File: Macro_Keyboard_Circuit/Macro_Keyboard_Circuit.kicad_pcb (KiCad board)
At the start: 2 copper layers, 115.2 x 117.1 mm, 49 parts, among them J1 OSTTC082162, J2 PRT-16766, SW1 SW_Push, SW10 SW_Push, SW11 SW_Push, SW12 SW_Push, SW2 SW_Push, SW3 SW_Push, SW4 SW_Push, SW5 SW_Push, SW6 SW_Push, SW7 SW_Push, SW8 SW_Push, SW9 SW_Push, U1 KY-040, U2 Adafruit KB2040, U3 KY-040, U4 KY-040

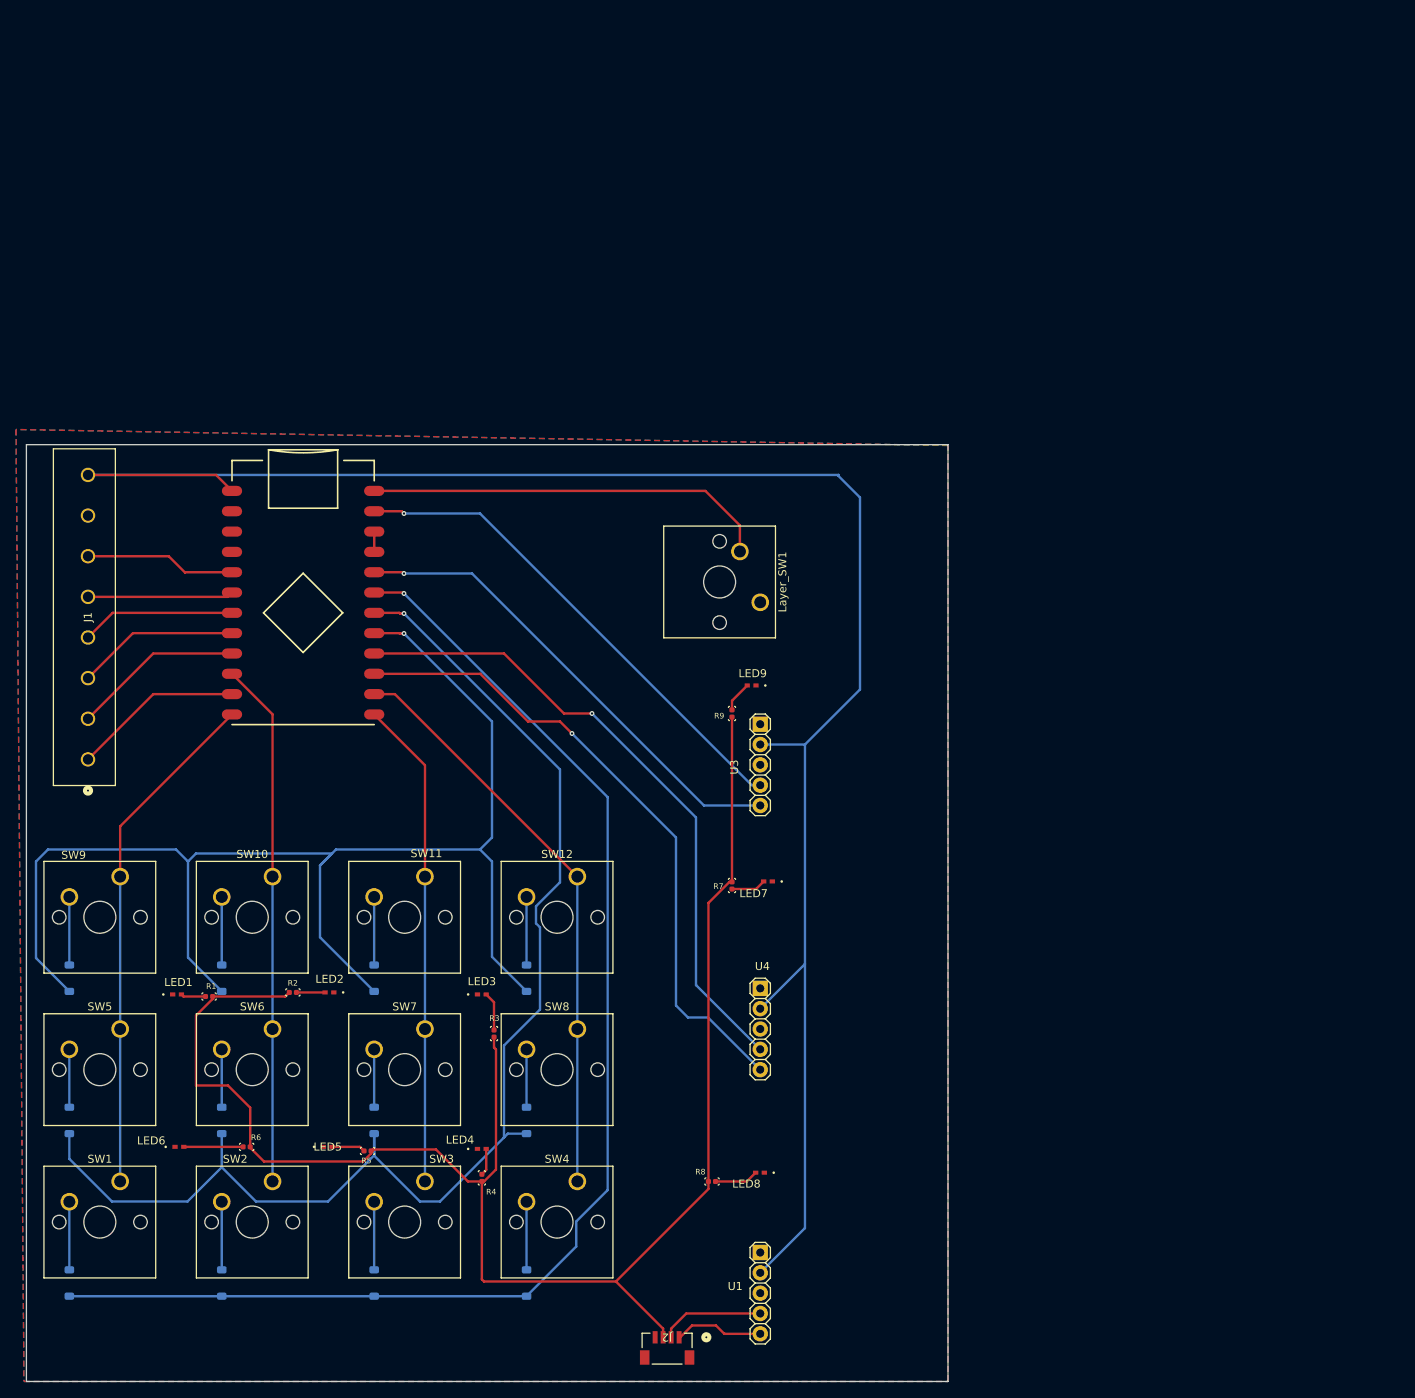
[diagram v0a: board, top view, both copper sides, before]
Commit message: Major revision to circuit due to change in acess to assembly tools. Finalized verson of PCB. Still need to update board codebase to reflect the new board configurations.
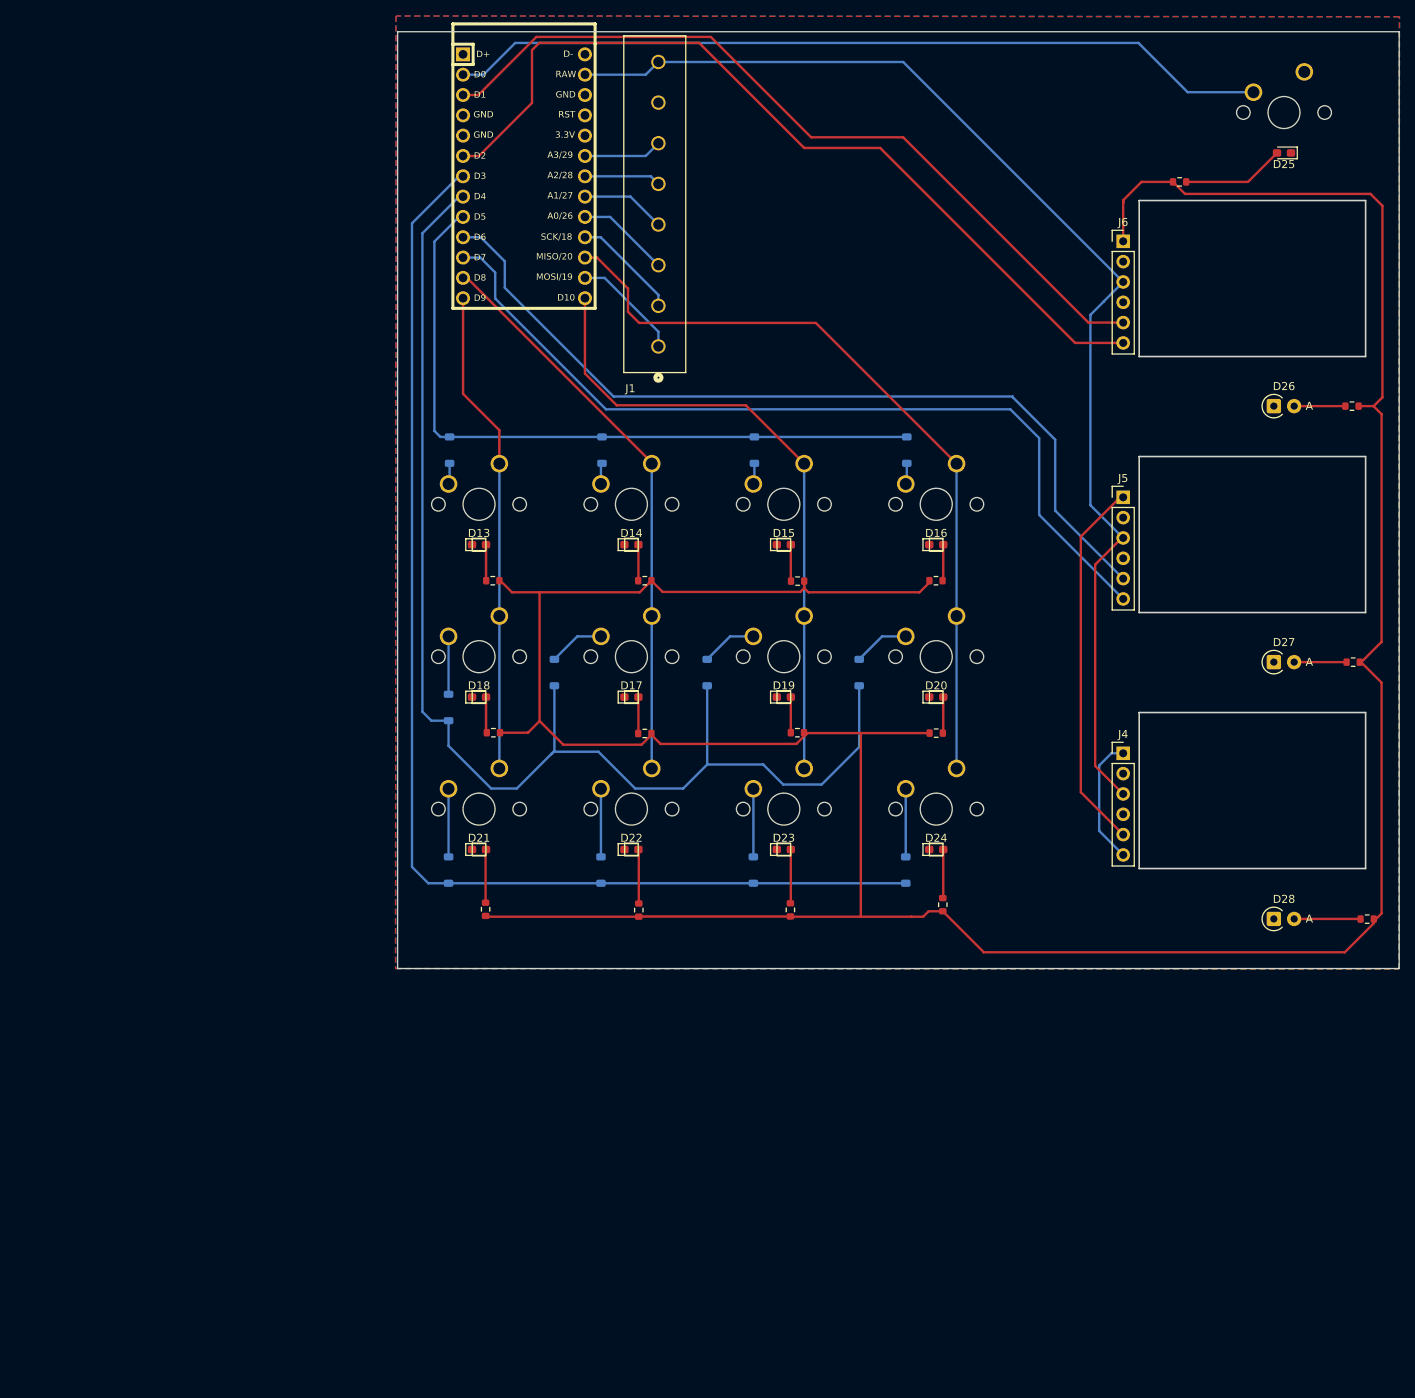
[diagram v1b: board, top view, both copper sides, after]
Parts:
- removed J2: PRT-16766, PRT_16766:CONN_BM04B-SRSS-TB_SPK
- removed LED1, LED2, LED3, LED4, LED5, LED6, LED7, LED8, LED9: HSMW-C280, HSMW_C280:LED_HSMW-C280_BRA
- removed U2: Adafruit KB2040, SparkFun-Board:ProMicroC
- removed U3, U4: KY-040, KY_040:KY_040_PORT
- added D13: LED, SW_Cherry_MX:D_0603_1608Metric_Pad1.05x0.95mm_HandSolder_cherrymx_silk, F.Cu at (77.9, 94.4)
- added D14: LED, SW_Cherry_MX:D_0603_1608Metric_Pad1.05x0.95mm_HandSolder_cherrymx_silk, F.Cu at (96.9, 94.4)
- added D15: LED, SW_Cherry_MX:D_0603_1608Metric_Pad1.05x0.95mm_HandSolder_cherrymx_silk, F.Cu at (116.0, 94.4)
- added D16: LED, SW_Cherry_MX:D_0603_1608Metric_Pad1.05x0.95mm_HandSolder_cherrymx_silk, F.Cu at (135.0, 94.4)
- added D17: LED, SW_Cherry_MX:D_0603_1608Metric_Pad1.05x0.95mm_HandSolder_cherrymx_silk, F.Cu at (96.9, 113.5)
- added D18: LED, SW_Cherry_MX:D_0603_1608Metric_Pad1.05x0.95mm_HandSolder_cherrymx_silk, F.Cu at (77.9, 113.5)
- added D19: LED, SW_Cherry_MX:D_0603_1608Metric_Pad1.05x0.95mm_HandSolder_cherrymx_silk, F.Cu at (116.0, 113.5)
- added D20: LED, SW_Cherry_MX:D_0603_1608Metric_Pad1.05x0.95mm_HandSolder_cherrymx_silk, F.Cu at (135.0, 113.5)
- added D21: LED, SW_Cherry_MX:D_0603_1608Metric_Pad1.05x0.95mm_HandSolder_cherrymx_silk, F.Cu at (77.9, 132.5)
- added D22: LED, SW_Cherry_MX:D_0603_1608Metric_Pad1.05x0.95mm_HandSolder_cherrymx_silk, F.Cu at (96.9, 132.5)
- added D23: LED, SW_Cherry_MX:D_0603_1608Metric_Pad1.05x0.95mm_HandSolder_cherrymx_silk, F.Cu at (116.0, 132.5)
- added D24: LED, SW_Cherry_MX:D_0603_1608Metric_Pad1.05x0.95mm_HandSolder_cherrymx_silk, F.Cu at (135.0, 132.5)
- added D25: LED, Diode_SMD:D_0603_1608Metric_Pad1.05x0.95mm_HandSolder, F.Cu at (178.5, 45.4)
- added D26: LED, Diode_THT:D_A-405_P2.54mm_Vertical_AnodeUp, F.Cu at (177.2, 77.1)
- added D27: LED, Diode_THT:D_A-405_P2.54mm_Vertical_AnodeUp, F.Cu at (177.2, 109.1)
- added D28: LED, Diode_THT:D_A-405_P2.54mm_Vertical_AnodeUp, F.Cu at (177.2, 141.2)
- added J4: Conn_01x06_Pin, Connector_PinHeader_2.54mm:PinHeader_1x06_P2.54mm_Vertical, F.Cu at (158.4, 120.5)
- added J5: Conn_01x06_Pin, Connector_PinHeader_2.54mm:PinHeader_1x06_P2.54mm_Vertical, F.Cu at (158.4, 88.5)
- added J6: Conn_01x06_Pin, Connector_PinHeader_2.54mm:PinHeader_1x06_P2.54mm_Vertical, F.Cu at (158.4, 56.5)
- added R10: 100, SparkFun-Resistor:R_0603_1608Metric, F.Cu at (97.8, 140.1)
- added R11: 100, SparkFun-Resistor:R_0603_1608Metric, F.Cu at (116.8, 140.1)
- added R12: 100, SparkFun-Resistor:R_0603_1608Metric, F.Cu at (135.8, 139.4)
- added R13: 100, SparkFun-Resistor:R_0603_1608Metric, F.Cu at (165.4, 49.0)
- added R14: 43, SparkFun-Resistor:R_0603_1608Metric, F.Cu at (187.0, 77.1)
- added R15: 43, SparkFun-Resistor:R_0603_1608Metric, F.Cu at (187.2, 109.1)
- added R16: 43, SparkFun-Resistor:R_0603_1608Metric, F.Cu at (188.9, 141.2)
- Layer_SW1, SW1, SW10, SW11, SW12, SW2, SW3, SW4, SW5, SW6, SW7, SW8, SW9: footprint Button_Switch_Keyboard:SW_Cherry_MX_1.00u_PCB -> SW_Cherry_MX:SW_Cherry_modified
- R1, R2, R3, R4, R5, R6, R7, R8, R9: value 33R -> 100; footprint RC0402FR-0733RL:R0402 -> SparkFun-Resistor:R_0603_1608Metric
- U1: value KY-040 -> kb2040; footprint KY_040:KY_040_PORT -> kb2040:kb2040
- moved U1 142.7 mm to (83.5, 47.1), turned to 0 degrees
- moved Layer_SW1 95.0 mm to (181.0, 35.3), turned to 0 degrees
- moved R4 93.8 mm to (135.0, 98.9), turned to 0 degrees
- moved J1 88.0 mm to (100.3, 69.6)
- moved D1 81.3 mm to (74.2, 82.6), turned to -90 degrees
- moved D2 81.3 mm to (93.2, 82.6), turned to -90 degrees
- moved D3 81.3 mm to (112.3, 82.6), turned to -90 degrees
- moved D4 81.3 mm to (131.3, 82.6), turned to -90 degrees
- moved D10 70.1 mm to (112.2, 135.1)
- moved D11 70.1 mm to (93.1, 135.1)
- moved D12 70.1 mm to (74.1, 135.1)
- moved D5 70.1 mm to (74.1, 114.8)
- moved D9 70.1 mm to (131.2, 135.1)
- moved SW1 70.1 mm to (80.4, 122.4)
- moved SW2 70.1 mm to (99.5, 122.4)
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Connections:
- J1 pad 1: Net-(U2-MOSI) -> Net-(U1-MOSI/19)
- J1 pad 2: Net-(U2-SCK) -> Net-(U1-SCK/18)
- J1 pad 3: Net-(U2-A0) -> Net-(U1-A0/26)
- J1 pad 4: Net-(U2-A1) -> Net-(U1-A1/27)
- J1 pad 5: Net-(U2-A2) -> Net-(U1-A2/28)
- J1 pad 6: Net-(U2-A3) -> Net-(U1-A3/29)
- J1 pad 8: Net-(U2-RAW_(5V)) -> Net-(J4-VCC)
- Layer_SW1 pad 2: Net-(U2-D0) -> Net-(U1-D0)
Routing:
- net Net-(U2-RAW_(5V)): track 232.2 -> 0.00 mm
- net Net-(J6-3V): track 201.1 -> 404.7 mm
- net Net-(J4-VCC): track 0.00 -> 149.7 mm
- net Net-(J6-CLK): track 0.00 -> 107.8 mm
- net Net-(J5-CLK): track 0.00 -> 107.7 mm
- net Net-(J5-DT): track 0.00 -> 107.4 mm
- net Net-(U1-D0): track 0.00 -> 103.0 mm
- net Net-(J6-DT): track 0.00 -> 100.3 mm
- net /Row1: track 172.2 -> 88.1 mm, vias 1 -> 0
- net Net-(U2-D7): track 81.0 -> 0.00 mm, vias 1 -> 0
- net Net-(U2-D6): track 81.0 -> 0.00 mm, vias 1 -> 0
- net Net-(U2-D1): track 62.4 -> 0.00 mm, vias 1 -> 0
- net Net-(U2-D2): track 60.3 -> 0.00 mm, vias 1 -> 0
- net Net-(U2-D0): track 50.8 -> 0.00 mm
- net Net-(J4-DT): track 0.00 -> 46.8 mm
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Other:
- board size 115.2 x 117.1 mm -> 125.2 x 117.1 mm
